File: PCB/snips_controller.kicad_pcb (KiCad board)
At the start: 4 copper layers, 35 x 99.9 mm, 93 parts

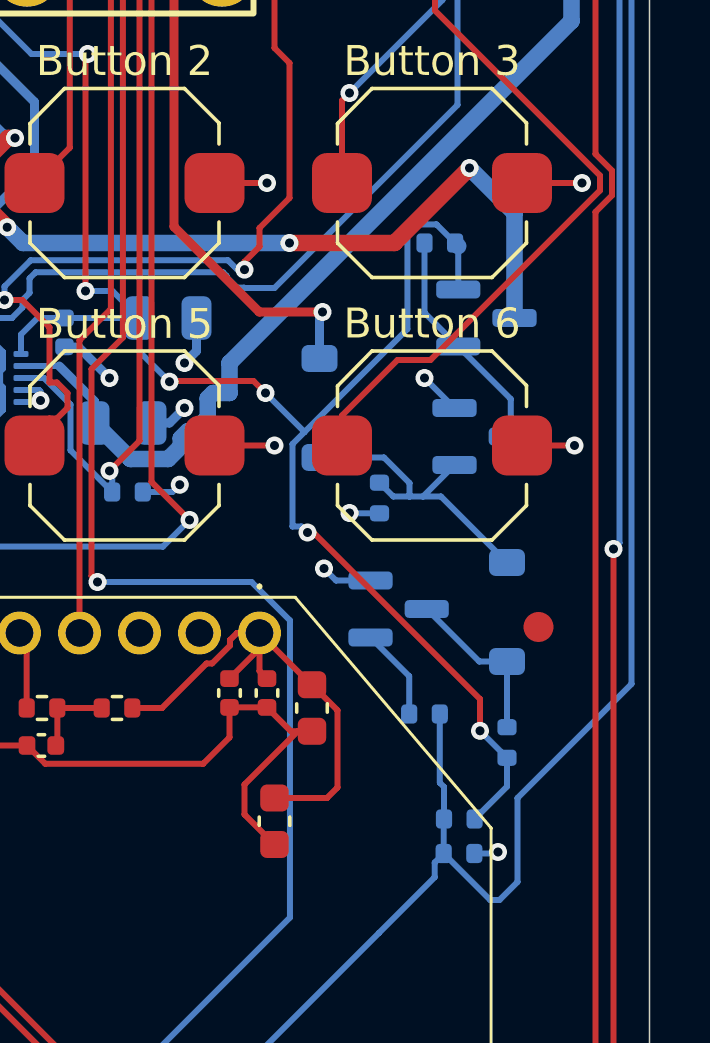
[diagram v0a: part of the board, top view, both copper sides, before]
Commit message: fix: latch gate-drive divider, floating buck EN, and missing accelerometer MPNs (#58)
Power latch, round 2 (found via cross-checking a third-party static-analysis
tool run against this project's own netlist and real component datasheets):

- R_LATCH_G1 raised 10kΩ -> 1MΩ. The prior value formed an unintended divider
  with R_INV_PU1 across D_OR1, leaving only ~0.3V at Q_LATCH1's gate on a
  press -- nowhere near enough to turn it on, meaning last round's inverter
  fix likely didn't actually latch on real hardware. Raising the pull-down
  instead of shrinking the pull-up avoids turning Q_INV1's idle state into a
  continuous mA-scale drain.
- R_INV_BASE1 repurposed from a series resistor (which shared current with
  R_BTN_PU1 and sagged the MCU's own button-sense read to ~1V) into its own
  dedicated 100k VSYS pull-up, decoupled via a new Schottky (D_INV_ISO1,
  BAT54W) so a press can still pull the base low without loading the shared
  sense node.
- Added R_PWR_EN_PD1 (100k to GND): the buck's EN pin had no pull-up or
  pull-down at all. TI's TLV62569 datasheet says not to leave it floating;
  Q_PWR1's drain is its only prior connection.

Also fills in MF/MPN for the 4 accelerometer parts (U_ACCEL1, C_ACCEL_1/2/3)
that were missing them, and retires the JLCPCB Basic-library matching
preference -- we're no longer targeting JLCPCB assembly for this board.

power_control_layout diagrams updated to match. Verified via kicad-cli sch
erc, sch export netlist, and pcb drc after every change; production files
regenerated.

Co-authored-by: Claude Sonnet 5 <noreply@anthropic.com>
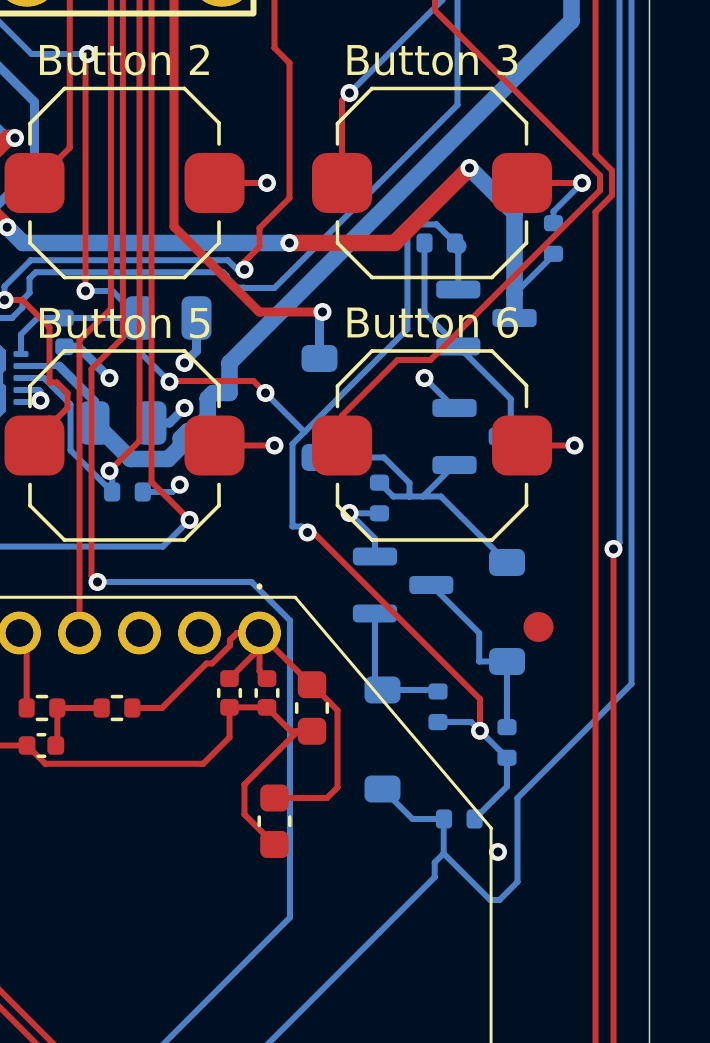
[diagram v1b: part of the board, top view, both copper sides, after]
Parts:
- removed R_PWR_SENSE1: 100kΩ, Resistor_SMD:R_0402_1005Metric
- added D_INV_ISO1: BAT54W, Diode_SMD:D_SOD-123, B.Cu at (146.1, 131.1)
- added R_PWR_EN_PD1: 100kΩ, Resistor_SMD:R_0402_1005Metric, B.Cu at (151.8, 114.3)
- Q_PWR1: value DMG2305UX -> AO3401A
- R_INV_BASE1: value 10kΩ -> 100kΩ
- R_LATCH_G1: value 10kΩ -> 1MΩ
- moved Q_INV1 0.81 mm to (146.8, 125.9)
- moved R_INV_BASE1 0.51 mm to (147.9, 130.0), turned to 90 degrees
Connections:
- R_INV_BASE1 pad 1: /MCU_Core/PWR_BTN_SENSE -> VSYS
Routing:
- net /Power_Buck/PWR_EN: track 27.8 -> 29.7 mm
- net VSYS: track 86.2 -> 87.7 mm
- net /Power_Control/PWR_BTN_INV_BASE: track 3.08 -> 4.52 mm
- net /MCU_Core/PWR_BTN_SENSE: track 135.2 -> 134.1 mm
- net GND: track 173.8 -> 174.9 mm, vias 43 -> 42
- net /Power_Control/PWR_BTN_TRIGGER: track 5.59 -> 6.33 mm

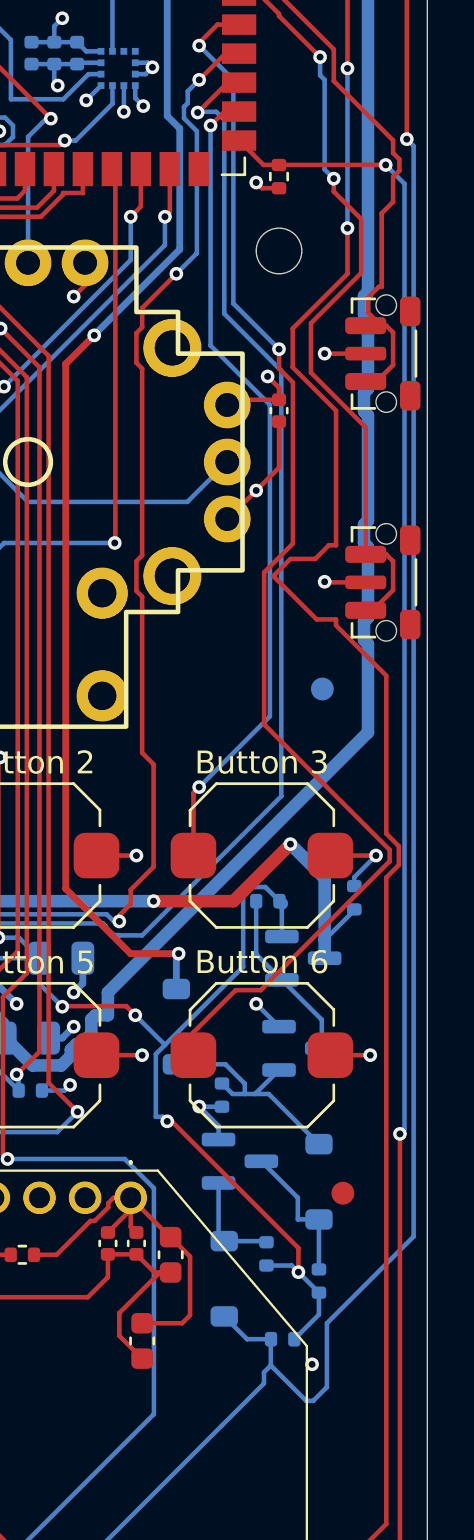
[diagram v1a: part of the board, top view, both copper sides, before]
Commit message: fix: keep button-sense within MCU rail, and add latch-gate margin at low battery (#59)
Both found by cross-checking a friend's static-analysis tool against our own
netlist and datasheets.

- R_BTN_PU1 now pulls up to 3V3 instead of VSYS. PWR_BTN_SENSE lands
  directly on GPIO2, whose ceiling is VDD+0.3V (~3.6V), but idled at VSYS
  (up to ~4.5V on USB). It also back-fed the unpowered 3V3 rail through the
  pin's clamp diode when the MCU was off. Safe now that R_INV_BASE1 gives the
  inverter its own VSYS pull-up, so R_BTN_PU1 no longer supplies it. A
  divider can't work across the 3.0-4.5V VSYS range (needs >=2.5V to read
  high but <=3.6V max).
- Q_LATCH1 swapped 2N7002 -> AO3400A. With realistic diode drop the gate
  reaches ~2.4V at VSYS=3.0V, which has no margin against the 2N7002's 2.5V
  worst-case threshold. AO3400A's Vgs(th) max is 1.45V (same SOT-23 G/S/D
  pinout, property-only change, no reroute).

Layout diagrams/docs updated (callouts D and H); production files
regenerated. ERC/DRC clean, all parts have MF/MPN.

Co-authored-by: Claude Sonnet 5 <noreply@anthropic.com>
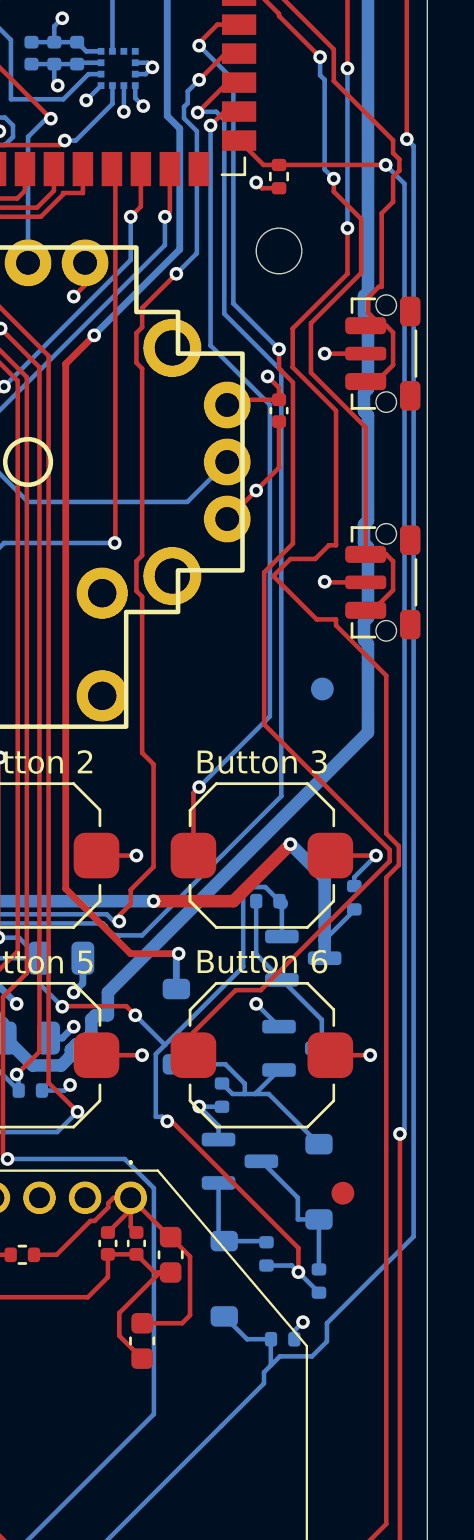
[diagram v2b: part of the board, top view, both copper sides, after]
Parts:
- Q_LATCH1: value 2N7002 -> AO3400A
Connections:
- R_BTN_PU1 pad 1: VSYS -> 3V3
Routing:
- net VSYS: track 87.7 -> 85.2 mm
- net /MCU_Core/PWR_BTN_SENSE: track 134.1 -> 131.6 mm
- net 3V3: track 65.5 -> 66.4 mm, vias 12 -> 13
- net GND: track 174.9 -> 174.8 mm, vias 42 -> 41
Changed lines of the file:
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@@
 			(layers "B.Cu" "B.Mask" "B.Paste")
 			(roundrect_rratio 0.25)
-			(net "VSYS")
+			(net "3V3")
 			(pintype "passive")
 		)
@@
 			)
 		)
-		(property "Value" "2N7002"
+		(property "Value" "AO3400A"
 			(at 0 -2.4 0)
 			(layer "B.Fab")
@@
 			)
 		)
-		(property "MF" "Jiangsu Changjing Electronics Technology Co., Ltd."
+		(property "MF" "Alpha & Omega Semicon"
 			(at 0 0 0)
 			(unlocked yes)
@@
 			)
 		)
-		(property "Manufacturer_Part_Number" "2N7002"
+		(property "Manufacturer_Part_Number" "AO3400A"
 			(at 0 0 0)
 			(unlocked yes)
@@
 			)
 		)
-		(property "LCSC" "C8545"
+		(property "LCSC" "C20917"
 			(at 0 0 0)
 			(unlocked yes)
@@
 	)
 	(via
+		(at 149.55 132.95)
+		(size 0.6)
+		(drill 0.3)
+		(layers "F.Cu" "B.Cu")
+		(net "3V3")
+	)
+	(via
 		(at 148 91.5)
 		(size 0.6)
@@
 	)
 	(segment
+		(start 149.17 133.33)
+		(end 149.55 132.95)
+		(width 0.2)
+		(layer "B.Cu")
+		(net "3V3")
+	)
+	(segment
+		(start 149.17 133.7)
+		(end 149.17 133.33)
+		(width 0.2)
+		(layer "B.Cu")
+		(net "3V3")
+	)
+	(segment
 		(start 122.025 109.05)
 		(end 122.025 107.975)
@@
 	)
 	(via
-		(at 149.95 134.8)
-		(size 0.6)
-		(drill 0.3)
-		(layers "F.Cu" "B.Cu")
-		(net "GND")
-	)
-	(via
 		(at 145 123.5)
 		(size 0.6)
@@
 	)
 	(segment
-		(start 149.9 134.85)
-		(end 149.95 134.8)
-		(width 0.2)
-		(layer "B.Cu")
-		(net "GND")
-	)
-	(segment
 		(start 133.45 120.070634)
 		(end 133.020634 120.5)
@@
 	)
 	(segment
-		(start 145.98 137.5)
-		(end 136.48 147)
+		(start 154.4 129.2)
+		(end 150.6 133)
 		(width 0.2)
 		(layer "B.Cu")
@@
 	)
 	(segment
-		(start 147.84 135.64)
-		(end 147.84 135.15)
+		(start 145.98 137.5)
+		(end 136.48 147)
 		(width 0.2)
 		(layer "B.Cu")
@@
 	(segment
 		(start 150.6 133)
-		(end 150.6 135.8)
+		(end 150.6 133.8)
 		(width 0.2)
 		(layer "B.Cu")
@@
 	(segment
 		(start 147.84 135.64)
-		(end 145.98 137.5)
+		(end 147.84 135.15)
 		(width 0.2)
 		(layer "B.Cu")
@@
 	)
 	(segment
-		(start 154.4 129.2)
-		(end 154.4 81.4)
+		(start 148.54 134.45)
+		(end 148.14 134.85)
+		(width 0.2)
+		(layer "B.Cu")
+		(net "/MCU_Core/PWR_BTN_SENSE")
+	)
+	(segment
+		(start 147.84 135.64)
+		(end 145.98 137.5)
 		(width 0.2)
 		(layer "B.Cu")
@@
 	)
 	(segment
-		(start 150.6 133)
-		(end 154.4 129.2)
+		(start 150.6 133.8)
+		(end 149.95 134.45)
 		(width 0.2)
 		(layer "B.Cu")
@@
 	)
 	(segment
-		(start 154.4 81.4)
-		(end 154.1 81.1)
-		(width 0.2)
-		(layer "B.Cu")
-		(net "/MCU_Core/PWR_BTN_SENSE")
-	)
-	(segment
 		(start 147.84 135.15)
 		(end 148.14 134.85)
@@
 	)
 	(segment
-		(start 148.15 133.7)
-		(end 147.1 133.7)
+		(start 154.1 81.1)
+		(end 154.4 81.4)
 		(width 0.2)
 		(layer "B.Cu")
@@
 	)
 	(segment
-		(start 150 136.4)
-		(end 149.69 136.4)
+		(start 149.95 134.45)
+		(end 148.54 134.45)
 		(width 0.2)
 		(layer "B.Cu")
@@
 	)
 	(segment
-		(start 125.063866 147)
-		(end 122.9845 149.079366)
+		(start 148.15 133.7)
+		(end 147.1 133.7)
 		(width 0.2)
 		(layer "B.Cu")
@@
 	)
 	(segment
-		(start 148.14 133.71)
-		(end 148.15 133.7)
+		(start 125.063866 147)
+		(end 122.9845 149.079366)
 		(width 0.2)
 		(layer "B.Cu")
@@
 	)
 	(segment
-		(start 122.9845 149.079366)
-		(end 122.9845 152.4845)
+		(start 154.4 81.4)
+		(end 154.4 129.2)
 		(width 0.2)
 		(layer "B.Cu")
@@
 	)
 	(segment
-		(start 150.6 135.8)
-		(end 150 136.4)
+		(start 148.14 133.71)
+		(end 148.15 133.7)
 		(width 0.2)
 		(layer "B.Cu")
@@
 	)
 	(segment
-		(start 149.69 136.4)
-		(end 148.14 134.85)
+		(start 122.9845 149.079366)
+		(end 122.9845 152.4845)
 		(width 0.2)
 		(layer "B.Cu")
@@
 	)
 	(segment
-		(start 150.25 132.62)
-		(end 149.17 133.7)
-		(width 0.2)
-		(layer "B.Cu")
-		(net "VSYS")
-	)
-	(segment
 		(start 149.35 130.76)
 		(end 150.25 131.66)
@@
 		(width 0.2)
 		(layer "B.Cu")
-		(net "VSYS")
-	)
-	(segment
-		(start 150.25 131.66)
-		(end 150.25 132.62)
-		(width 0.2)
-		(layer "B.Cu")

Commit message: fix: add C_LATCH_G1 to stop a ~2ms PWR_EN blip on battery insertion (#60)
* fix: add C_LATCH_G1 to stop a ~2ms PWR_EN blip on battery insertion

There's no physical board yet, so this was found by simulating the
button/inverter/latch circuit in ngspice (KiCad's bundled libngspice) after a
validator run claimed the board would power itself on. That claim doesn't hold
(off-state base sits ~0.6-0.7V because the button node is only grounded
through R_BTN_PU1, and a fast 3V3 collapse at shutdown never lifts the latch
gate), but the simulation did show a real, minor transient: on battery
insertion Q_INV1 isn't conducting until C_DBNC1 charges through D_INV_ISO1, so
PWR_LATCH_G briefly rises to ~VSYS-0.6V and PWR_EN pulses ~1.9ms. This
existed before the 3V3 pull-up change too (~1.4ms).

C_LATCH_G1 (100nF 0402, same part as C_DBNC1) from PWR_LATCH_G to GND slows
the gate rise so the transient peaks at ~0.3V, under the AO3400A's minimum
threshold, at a cost of 4-8ms of press latency. 100nF chosen over 47nF, which
peaked at ~0.65V, right at a minimum-threshold part.

Layout diagrams/docs updated (callout I, routing step 8); production files
regenerated. ERC/DRC clean, all parts have MF/MPN.

Co-Authored-By: Claude Sonnet 5 <noreply@anthropic.com>

* chore: add SPICE check for the power latch, and commit KiCad settings

- scripts/spice/latch_sim.py: ngspice (KiCad's bundled libngspice) check of the
  soft-latch with pass/fail assertions for battery insertion, a press across
  supply/FET-threshold corners, and shutdown. Reproduces the insertion blip
  fixed by C_LATCH_G1 (fails with --cap 0) and the gate-margin reason for
  choosing 100nF over 47nF. README documents what is and isn't modeled.
- PCB/snips_controller.kicad_pro: KiCad's reordered used-designators list.

Co-Authored-By: Claude Sonnet 5 <noreply@anthropic.com>

---------

Co-authored-by: Claude Sonnet 5 <noreply@anthropic.com>
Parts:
- added C_LATCH_G1: 100nF, Capacitor_SMD:C_0402_1005Metric, B.Cu at (146.4, 120.3)
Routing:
- net GND: track 174.8 -> 176.2 mm
- net /Power_Control/PWR_LATCH_G: track 10.6 -> 11.7 mm
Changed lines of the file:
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@@
 	(footprint "Capacitor_SMD:C_0402_1005Metric"
 		(layer "B.Cu")
+		(at 146.45 120.28 -90)
+		(descr "Capacitor SMD 0402 (1005 Metric), square (rectangular) end terminal, IPC-7351 nominal, (Body size source: IPC-SM-782 page 76, https://www.pcb-3d.com/wordpress/wp-content/uploads/ipc-sm-782a_amendment_1_and_2.pdf)")
+		(tags "capacitor")
+		(property "Reference" "C_LATCH_G1"
+			(at 0 1.16 90)
+			(layer "B.SilkS")
+			(hide yes)
+			(effects
+				(font
+					(size 1 1)
+					(thickness 0.15)
+				)
+				(justify mirror)
+			)
+		)
+		(property "Value" "100nF"
+			(at 0 -1.16 90)
+			(layer "B.Fab")
+			(effects
+				(font
+					(size 1 1)
+					(thickness 0.15)
+				)
+				(justify mirror)
+			)
+		)
+		(property "Datasheet" ""
+			(at 0 0 90)
+			(layer "B.Fab")
+			(hide yes)
+			(effects
+				(font
+					(size 1.27 1.27)
+				)
+				(justify mirror)
+			)
+		)
+		(property "Description" "Unpolarized capacitor"
+			(at 0 0 90)
+			(layer "B.Fab")
+			(hide yes)
+			(effects
+				(font
+					(size 1.27 1.27)
+				)
+				(justify mirror)
+			)
+		)
+		(property "KiLib_Generator" "SMD_2terminal_chip_molded"
+			(at 0 0 90)
+			(layer "B.SilkS")
+			(hide yes)
+			(effects
+				(font
+					(size 1 1)
+					(thickness 0.15)
+				)
+				(justify mirror)
+			)
+		)
+		(property "MF" "Samsung Electro-Mechanics"
+			(at 0 0 90)
+			(unlocked yes)
+			(layer "B.Fab")
+			(hide yes)
+			(effects
+				(font
+					(size 1 1)
+					(thickness 0.15)
+				)
+				(justify mirror)
+			)
+		)
+		(property "Manufacturer_Part_Number" "CL05B104KO5NNNC"
+			(at 0 0 90)
+			(unlocked yes)
+			(layer "B.Fab")
+			(hide yes)
+			(effects
+				(font
+					(size 1 1)
+					(thickness 0.15)
+				)
+				(justify mirror)
+			)
+		)
+		(property "LCSC" "C1525"
+			(at 0 0 90)
+			(unlocked yes)
+			(layer "B.Fab")
+			(hide yes)
+			(effects
+				(font
+					(size 1 1)
+					(thickness 0.15)
+				)
+				(justify mirror)
+			)
+		)
+		(property ki_fp_filters "C_*")
+		(sheetname "/Power_Control/")
+		(sheetfile "power_control.kicad_sch")
+		(units
+			(unit
+				(name "A")
+				(pins "1" "2")
+			)
+		)
+		(attr smd)
+		(duplicate_pad_numbers_are_jumpers no)
+		(fp_line
+			(start -0.107836 0.36)
+			(end 0.107836 0.36)
+			(stroke
+				(width 0.12)
+				(type solid)
+			)
+			(layer "B.SilkS")
+		)
+		(fp_line
+			(start -0.107836 -0.36)
+			(end 0.107836 -0.36)
+			(stroke
+				(width 0.12)
+				(type solid)
+			)
+			(layer "B.SilkS")
+		)
+		(fp_rect
+			(start -0.91 0.46)
+			(end 0.91 -0.46)
+			(stroke
+				(width 0.05)
+				(type solid)
+			)
+			(fill no)
+			(layer "B.CrtYd")
+		)
+		(fp_rect
+			(start -0.5 0.25)
+			(end 0.5 -0.25)
+			(stroke
+				(width 0.1)
+				(type solid)
+			)
+			(fill no)
+			(layer "B.Fab")
+		)
+		(fp_text user "${REFERENCE}"
+			(at 0 0 90)
+			(layer "B.Fab")
+			(effects
+				(font
+					(size 0.25 0.25)
+					(thickness 0.04)
+				)
+				(justify mirror)
+			)
+		)
+		(pad "1" smd roundrect
+			(at -0.48 0 270)
+			(size 0.56 0.62)
+			(layers "B.Cu" "B.Mask" "B.Paste")
+			(roundrect_rratio 0.25)
+			(net "GND")
+			(pintype "passive")
+		)
+		(pad "2" smd roundrect
+			(at 0.48 0 270)
+			(size 0.56 0.62)
+			(layers "B.Cu" "B.Mask" "B.Paste")
+			(roundrect_rratio 0.25)
+			(net "/Power_Control/PWR_LATCH_G")
+			(pintype "passive")
+		)
+		(embedded_fonts no)
+		(model "${KICAD10_3DMODEL_DIR}/Capacitor_SMD.3dshapes/C_0402_1005Metric.step"
+			(offset
+				(xyz 0 0 0)
+			)
+			(scale
+				(xyz 1 1 1)
+			)
+			(rotate
+				(xyz 0 0 0)
+			)
+		)
+	)
+	(footprint "Capacitor_SMD:C_0402_1005Metric"
+		(layer "B.Cu")
 		(at 151.52 66 180)
 		(descr "Capacitor SMD 0402 (1005 Metric), square (rectangular) end terminal, IPC-7351 nominal, (Body size source: IPC-SM-782 page 76, https://www.pcb-3d.com/wordpress/wp-content/uploads/ipc-sm-782a_amendment_1_and_2.pdf)")
@@
 	)
 	(segment
+		(start 146.7 119.8)
+		(end 147.5 119)
+		(width 0.2)
+		(layer "B.Cu")
+		(net "GND")
+	)
+	(segment
 		(start 126.1 118)
 		(end 125 118)
@@
 	)
 	(segment
+		(start 146.45 119.8)
+		(end 146.7 119.8)
+		(width 0.2)
+		(layer "B.Cu")
+		(net "GND")
+	)
+	(segment
 		(start 139 120.5)
 		(end 139.5 120)
@@
 	)
 	(segment
+		(start 146.45 121.35)
+		(end 146.15 121.65)
+		(width 0.2)
+		(layer "B.Cu")
+		(net "/Power_Control/PWR_LATCH_G")
+	)
+	(segment
 		(start 147.45 122.95)
 		(end 148.5 121.9)
@@
 		(width 0.2)
 		(layer "B.Cu")
+		(net "/Power_Control/PWR_LATCH_G")
+	)
+	(segment
+		(start 146.45 120.76)
+		(end 146.45 121.35)
+		(width 0.2)
+		(layer "B.Cu")
